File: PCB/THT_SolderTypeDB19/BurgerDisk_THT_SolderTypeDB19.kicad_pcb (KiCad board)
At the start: 2 copper layers, 93.7 x 67.6 mm, 18 parts, among them J1 Daisy port in, J2 MicroSD module, J3 UART, J4 Daisy port out, U1 PC817

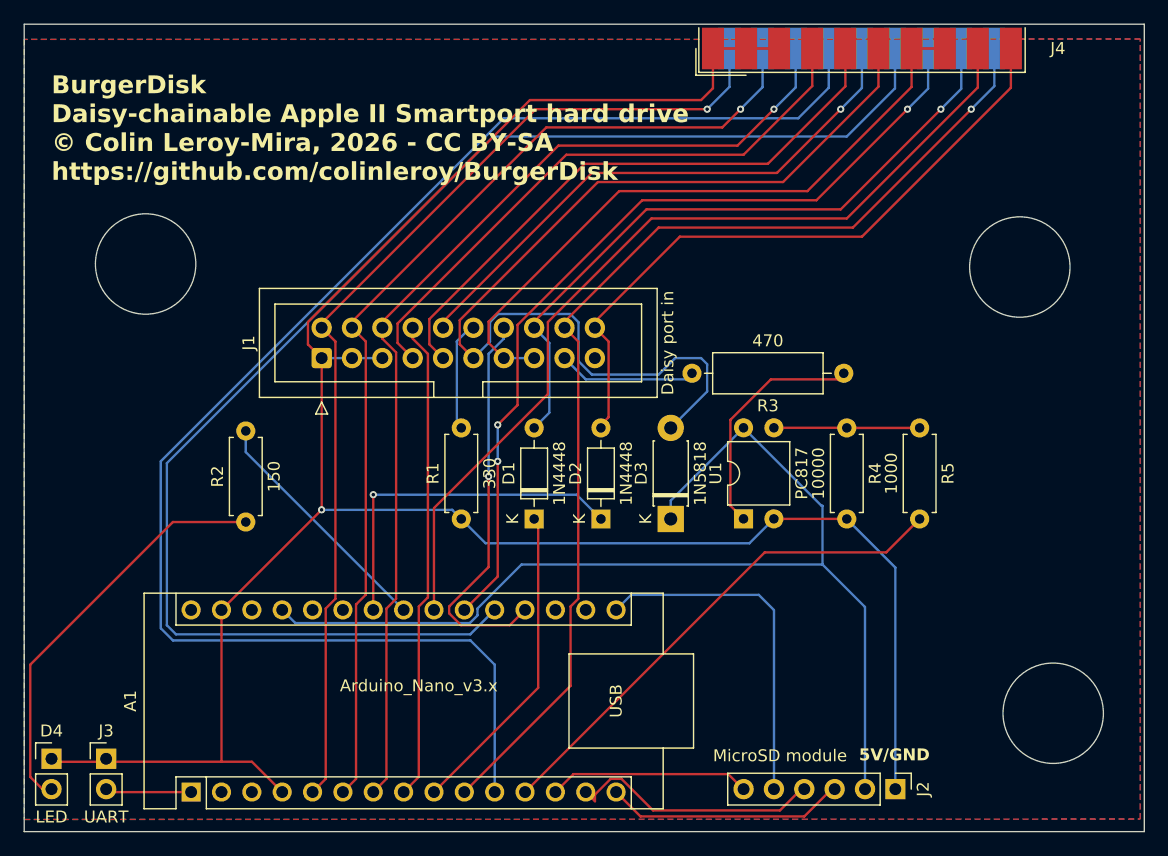
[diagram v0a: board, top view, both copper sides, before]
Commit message: Wider tracks for power
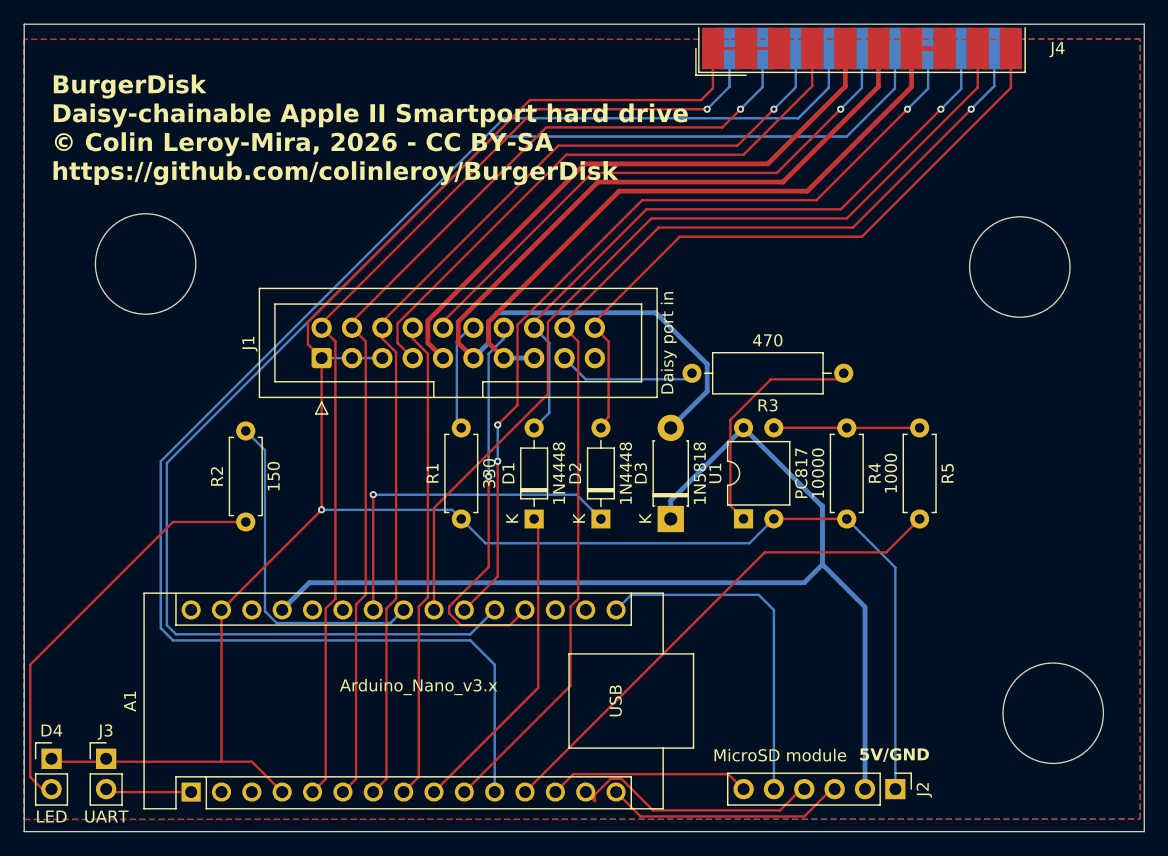
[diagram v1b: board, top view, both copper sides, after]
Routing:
- net Net-(A1-A4): track 20.4 -> 28.2 mm
- net 5V_apple2: track 83.4 -> 80.6 mm
- net 5V_burgerDisk: track 92.7 -> 91.4 mm
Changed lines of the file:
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@@
   (segment (start 100.076 83.058) (end 117.094 83.058) (width 0.2) (layer "B.Cu") (net 19))
   (segment (start 117.094 83.058) (end 119.126 85.09) (width 0.2) (layer "B.Cu") (net 19))
-  (segment (start 108.151635 93.8) (end 108.796 93.155635) (width 0.2) (layer "B.Cu") (net 20))
-  (segment (start 137.589 83.99) (end 131.059 77.46) (width 0.2) (layer "B.Cu") (net 20))
-  (segment (start 93.556 93.8) (end 108.151635 93.8) (width 0.2) (layer "B.Cu") (net 20))
-  (segment (start 92.456 92.7) (end 93.556 93.8) (width 0.2) (layer "B.Cu") (net 20))
-  (segment (start 124.968 85.09) (end 124.968 83.551) (width 0.2) (layer "B.Cu") (net 20))
-  (segment (start 141.224 92.456) (end 141.224 107.696) (width 0.2) (layer "B.Cu") (net 20))
-  (segment (start 124.968 83.551) (end 131.059 77.46) (width 0.2) (layer "B.Cu") (net 20))
-  (segment (start 137.668 88.9) (end 137.668 83.99) (width 0.2) (layer "B.Cu") (net 20))
-  (segment (start 137.668 88.9) (end 141.224 92.456) (width 0.2) (layer "B.Cu") (net 20))
-  (segment (start 108.796 93.155635) (end 108.796 92.584365) (width 0.2) (layer "B.Cu") (net 20))
-  (segment (start 112.480365 88.9) (end 137.668 88.9) (width 0.2) (layer "B.Cu") (net 20))
-  (segment (start 108.796 92.584365) (end 112.480365 88.9) (width 0.2) (layer "B.Cu") (net 20))
-  (segment (start 137.668 83.99) (end 137.589 83.99) (width 0.2) (layer "B.Cu") (net 20))
+  (segment (start 137.589 83.99) (end 131.059 77.46) (width 0.4) (layer "B.Cu") (net 20))
+  (segment (start 124.968 85.09) (end 124.968 83.551) (width 0.4) (layer "B.Cu") (net 20))
+  (segment (start 141.224 92.456) (end 141.224 107.696) (width 0.4) (layer "B.Cu") (net 20))
+  (segment (start 124.968 83.551) (end 131.059 77.46) (width 0.4) (layer "B.Cu") (net 20))
+  (segment (start 137.668 88.9) (end 137.668 83.99) (width 0.4) (layer "B.Cu") (net 20))
+  (segment (start 137.668 88.9) (end 141.224 92.456) (width 0.4) (layer "B.Cu") (net 20))
+  (segment (start 136.144 90.424) (end 137.668 88.9) (width 0.4) (layer "B.Cu") (net 20))
+  (segment (start 92.456 92.7) (end 94.732 90.424) (width 0.4) (layer "B.Cu") (net 20))
+  (segment (start 94.732 90.424) (end 136.144 90.424) (width 0.4) (layer "B.Cu") (net 20))
+  (segment (start 137.668 83.99) (end 137.589 83.99) (width 0.4) (layer "B.Cu") (net 20))
   (segment (start 122.936 59.182) (end 113.538 68.58) (width 0.2) (layer "F.Cu") (net 21))
   (segment (start 147.574 50.8) (end 139.192 59.182) (width 0.2) (layer "F.Cu") (net 21))
@@
   (segment (start 140.97 61.468) (end 125.73 61.468) (width 0.2) (layer "F.Cu") (net 22))
   (segment (start 119.768 70.238) (end 119.768 76.574) (width 0.2) (layer "F.Cu") (net 22))
-  (segment (start 107.308 68.46) (end 107.308 70.478) (width 0.2) (layer "F.Cu") (net 23))
-  (segment (start 142.35 45.72) (end 142.35 48.912) (width 0.2) (layer "F.Cu") (net 23))
-  (segment (start 107.308 70.478) (end 108.458 71.628) (width 0.2) (layer "F.Cu") (net 23))
-  (segment (start 118.872 56.896) (end 107.308 68.46) (width 0.2) (layer "F.Cu") (net 23))
-  (segment (start 142.35 48.912) (end 134.366 56.896) (width 0.2) (layer "F.Cu") (net 23))
-  (segment (start 134.366 56.896) (end 118.872 56.896) (width 0.2) (layer "F.Cu") (net 23))
-  (segment (start 127.508 71.628) (end 128.016 72.136) (width 0.2) (layer "B.Cu") (net 23))
-  (segment (start 117.249843 68.633497) (end 117.249843 71.886189) (width 0.2) (layer "B.Cu") (net 23))
-  (segment (start 128.016 72.136) (end 128.016 74.422) (width 0.2) (layer "B.Cu") (net 23))
-  (segment (start 109.848 70.238) (end 109.848 68.611654) (width 0.2) (layer "B.Cu") (net 23))
-  (segment (start 128.016 74.422) (end 124.968 77.47) (width 0.2) (layer "B.Cu") (net 23))
-  (segment (start 123.952 73.006) (end 125.33 71.628) (width 0.2) (layer "B.Cu") (net 23))
-  (segment (start 125.33 71.628) (end 127.508 71.628) (width 0.2) (layer "B.Cu") (net 23))
-  (segment (start 109.848 68.611654) (end 110.521654 67.938) (width 0.2) (layer "B.Cu") (net 23))
-  (segment (start 117.249843 71.886189) (end 118.369654 73.006) (width 0.2) (layer "B.Cu") (net 23))
-  (segment (start 116.554346 67.938) (end 117.249843 68.633497) (width 0.2) (layer "B.Cu") (net 23))
-  (segment (start 110.521654 67.938) (end 116.554346 67.938) (width 0.2) (layer "B.Cu") (net 23))
-  (segment (start 108.458 71.628) (end 109.848 70.238) (width 0.2) (layer "B.Cu") (net 23))
-  (segment (start 118.369654 73.006) (end 123.952 73.006) (width 0.2) (layer "B.Cu") (net 23))
+  (segment (start 107.188 68.58) (end 107.188 70.358) (width 0.4) (layer "F.Cu") (net 23))
+  (segment (start 107.188 70.358) (end 108.458 71.628) (width 0.4) (layer "F.Cu") (net 23))
+  (segment (start 142.35 45.72) (end 142.35 48.912) (width 0.4) (layer "F.Cu") (net 23))
+  (segment (start 118.872 56.896) (end 107.188 68.58) (width 0.4) (layer "F.Cu") (net 23))
+  (segment (start 134.366 56.896) (end 118.872 56.896) (width 0.4) (layer "F.Cu") (net 23))
+  (segment (start 142.35 48.912) (end 134.366 56.896) (width 0.4) (layer "F.Cu") (net 23))
+  (segment (start 128.016 74.422) (end 124.968 77.47) (width 0.4) (layer "B.Cu") (net 23))
+  (segment (start 110.47 67.838) (end 123.718 67.838) (width 0.4) (layer "B.Cu") (net 23))
+  (segment (start 108.458 71.628) (end 109.728 70.358) (width 0.4) (layer "B.Cu") (net 23))
+  (segment (start 109.728 68.58) (end 110.47 67.838) (width 0.4) (layer "B.Cu") (net 23))
+  (segment (start 109.728 70.358) (end 109.728 68.58) (width 0.4) (layer "B.Cu") (net 23))
+  (segment (start 128.016 72.136) (end 128.016 74.422) (width 0.4) (layer "B.Cu") (net 23))
+  (segment (start 123.718 67.838) (end 128.016 72.136) (width 0.4) (layer "B.Cu") (net 23))
   (segment (start 102.108 68.731654) (end 102.108 70.358) (width 0.2) (layer "F.Cu") (net 24))
   (segment (start 136.81 45.72) (end 136.81 48.864) (width 0.2) (layer "F.Cu") (net 24))
@@
   (segment (start 131.064 54.61) (end 116.229654 54.61) (width 0.2) (layer "F.Cu") (net 24))
   (segment (start 102.108 70.358) (end 103.378 71.628) (width 0.2) (layer "F.Cu") (net 24))
-  (segment (start 104.768 70.478) (end 105.918 71.628) (width 0.2) (layer "F.Cu") (net 25))
-  (segment (start 139.58 48.888) (end 133.096 55.372) (width 0.2) (layer "F.Cu") (net 25))
-  (segment (start 139.58 45.72) (end 139.58 48.888) (width 0.2) (layer "F.Cu") (net 25))
-  (segment (start 117.767654 55.372) (end 104.768 68.371654) (width 0.2) (layer "F.Cu") (net 25))
-  (segment (start 133.096 55.372) (end 117.767654 55.372) (width 0.2) (layer "F.Cu") (net 25))
-  (segment (start 104.768 68.371654) (end 104.768 70.478) (width 0.2) (layer "F.Cu") (net 25))
-  (segment (start 109.728 68.58) (end 109.728 70.358) (width 0.2) (layer "F.Cu") (net 26))
-  (segment (start 120.65 57.658) (end 109.728 68.58) (width 0.2) (layer "F.Cu") (net 26))
-  (segment (start 145.12 45.72) (end 145.12 48.936) (width 0.2) (layer "F.Cu") (net 26))
-  (segment (start 109.728 70.358) (end 110.998 71.628) (width 0.2) (layer "F.Cu") (net 26))
-  (segment (start 136.398 57.658) (end 120.65 57.658) (width 0.2) (layer "F.Cu") (net 26))
-  (segment (start 145.12 48.936) (end 136.398 57.658) (width 0.2) (layer "F.Cu") (net 26))
-  (segment (start 145.12 45.72) (end 147.89 45.72) (width 0.2) (layer "F.Cu") (net 26))
-  (segment (start 113.538 71.628) (end 110.998 71.628) (width 0.2) (layer "B.Cu") (net 26))
+  (segment (start 117.767654 55.372) (end 104.648 68.491654) (width 0.4) (layer "F.Cu") (net 25))
+  (segment (start 139.58 45.72) (end 139.58 48.888) (width 0.4) (layer "F.Cu") (net 25))
+  (segment (start 104.648 68.491654) (end 104.648 70.358) (width 0.4) (layer "F.Cu") (net 25))
+  (segment (start 133.096 55.372) (end 117.767654 55.372) (width 0.4) (layer "F.Cu") (net 25))
+  (segment (start 104.648 70.358) (end 105.918 71.628) (width 0.4) (layer "F.Cu") (net 25))
+  (segment (start 139.58 48.888) (end 133.096 55.372) (width 0.4) (layer "F.Cu") (net 25))
+  (segment (start 109.728 68.58) (end 109.728 70.358) (width 0.4) (layer "F.Cu") (net 26))
+  (segment (start 120.65 57.658) (end 109.728 68.58) (width 0.4) (layer "F.Cu") (net 26))
+  (segment (start 145.12 45.72) (end 145.12 48.936) (width 0.4) (layer "F.Cu") (net 26))
+  (segment (start 109.728 70.358) (end 110.998 71.628) (width 0.4) (layer "F.Cu") (net 26))
+  (segment (start 136.398 57.658) (end 120.65 57.658) (width 0.4) (layer "F.Cu") (net 26))
+  (segment (start 145.12 48.936) (end 136.398 57.658) (width 0.4) (layer "F.Cu") (net 26))
+  (segment (start 145.12 45.72) (end 147.89 45.72) (width 0.4) (layer "F.Cu") (net 26))
+  (segment (start 113.538 71.628) (end 110.998 71.628) (width 0.4) (layer "B.Cu") (net 26))
   (segment (start 117.856 73.406) (end 126.238 73.406) (width 0.2) (layer "B.Cu") (net 27))
   (segment (start 126.238 73.406) (end 126.746 72.898) (width 0.2) (layer "B.Cu") (net 27))
@@
   (segment (start 71.374 97.282) (end 83.312 85.344) (width 0.2) (layer "F.Cu") (net 41))
   (segment (start 71.374 106.68) (end 71.374 97.282) (width 0.2) (layer "F.Cu") (net 41))
-  (segment (start 89.408 79.492) (end 102.616 92.7) (width 0.2) (layer "B.Cu") (net 42))
-  (segment (start 89.408 77.724) (end 89.408 79.492) (width 0.2) (layer "B.Cu") (net 42))
+  (segment (start 92.000365 93.8) (end 91.016 92.815635) (width 0.2) (layer "B.Cu") (net 42))
+  (segment (start 91.016 92.815635) (end 91.016 79.332) (width 0.2) (layer "B.Cu") (net 42))
+  (segment (start 102.616 92.7) (end 101.516 93.8) (width 0.2) (layer "B.Cu") (net 42))
+  (segment (start 101.516 93.8) (end 92.000365 93.8) (width 0.2) (layer "B.Cu") (net 42))
+  (segment (start 91.016 79.332) (end 89.408 77.724) (width 0.2) (layer "B.Cu") (net 42))
   (zone (net 2) (net_name "GND") (layers "F&B.Cu") (hatch edge 0.5)
     (connect_pads (clearance 0.5))
     (min_thickness 0.25) (filled_areas_thickness no)
-    (fill yes (thermal_gap 0.5) (thermal_bridge_width 0.5))
+    (fill (thermal_gap 0.5) (thermal_bridge_width 0.5))
     (polygon
       (pts
